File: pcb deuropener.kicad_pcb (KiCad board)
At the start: 2 copper layers, 54.6 x 86.4 mm, 34 parts, among them J1 Conn_01x02, J10 Conn_01x03, J11 Barrel_Jack_Switch, J12 Conn_01x08, J13 Conn_01x02, J14 Conn_01x02, J2 Conn_01x02, J3 Conn_01x02, J4 Conn_01x02, J5 Conn_01x02, P8 BeagleBone_Black_Header, P9 BeagleBone_Black_Header, Q1 STU60N3LH5, Q2 STU60N3LH5, U1 TSR_1-2450

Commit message: A lot of changes for rev0.02 and fix for issue #2
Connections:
- net IO-P8_13-UI_TriLED1r renamed IO-P8_13-UI_DuoLED1r
- net IO-P8_19-UI_TriLED1g renamed IO-P8_19-UI_DuoLED1g
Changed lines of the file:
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@@
   (net 25 IO-P8_18-Button2)
   (net 26 IO-P8_17-Button1)
-  (net 27 IO-P8_19-UI_TriLED1g)
-  (net 28 IO-P8_13-UI_TriLED1r)
+  (net 27 IO-P8_19-UI_DuoLED1g)
+  (net 28 IO-P8_13-UI_DuoLED1r)
   (net 29 IO-P8_09-Buzzer)
   (net 30 IO-P9_16-UILED2)
@@
     (add_net Earth)
     (add_net IO-P8_09-Buzzer)
-    (add_net IO-P8_13-UI_TriLED1r)
+    (add_net IO-P8_13-UI_DuoLED1r)
     (add_net IO-P8_17-Button1)
     (add_net IO-P8_18-Button2)
-    (add_net IO-P8_19-UI_TriLED1g)
+    (add_net IO-P8_19-UI_DuoLED1g)
     (add_net IO-P9_12-Solenoid)
     (add_net IO-P9_14-UILED1)
@@
     (pad 20 thru_hole oval (at 2.54 22.86) (size 1.7272 1.7272) (drill 1.016) (layers *.Cu *.Mask F.SilkS))
     (pad 19 thru_hole oval (at 0 22.86) (size 1.7272 1.7272) (drill 1.016) (layers *.Cu *.Mask F.SilkS)
-      (net 27 IO-P8_19-UI_TriLED1g))
+      (net 27 IO-P8_19-UI_DuoLED1g))
     (pad 18 thru_hole oval (at 2.54 20.32) (size 1.7272 1.7272) (drill 1.016) (layers *.Cu *.Mask F.SilkS)
       (net 25 IO-P8_18-Button2))
@@
     (pad 14 thru_hole oval (at 2.54 15.24) (size 1.7272 1.7272) (drill 1.016) (layers *.Cu *.Mask F.SilkS))
     (pad 13 thru_hole oval (at 0 15.24) (size 1.7272 1.7272) (drill 1.016) (layers *.Cu *.Mask F.SilkS)
-      (net 28 IO-P8_13-UI_TriLED1r))
+      (net 28 IO-P8_13-UI_DuoLED1r))
     (pad 12 thru_hole oval (at 2.54 12.7) (size 1.7272 1.7272) (drill 1.016) (layers *.Cu *.Mask F.SilkS))
     (pad 11 thru_hole oval (at 0 12.7) (size 1.7272 1.7272) (drill 1.016) (layers *.Cu *.Mask F.SilkS))
@@
     (fp_line (start 1.93 -1.25) (end 1.93 1.25) (layer F.Fab) (width 0.1))
     (pad 2 thru_hole oval (at 10.16 0 90) (size 1.6 1.6) (drill 0.8) (layers *.Cu *.Mask)
-      (net 28 IO-P8_13-UI_TriLED1r))
+      (net 28 IO-P8_13-UI_DuoLED1r))
     (pad 1 thru_hole circle (at 0 0 90) (size 1.6 1.6) (drill 0.8) (layers *.Cu *.Mask)
       (net 12 "Net-(J10-Pad1)"))
@@
     (fp_line (start 1.93 -1.25) (end 1.93 1.25) (layer F.Fab) (width 0.1))
     (pad 2 thru_hole oval (at 10.16 0 90) (size 1.6 1.6) (drill 0.8) (layers *.Cu *.Mask)
-      (net 27 IO-P8_19-UI_TriLED1g))
+      (net 27 IO-P8_19-UI_DuoLED1g))
     (pad 1 thru_hole circle (at 0 0 90) (size 1.6 1.6) (drill 0.8) (layers *.Cu *.Mask)
       (net 13 "Net-(J10-Pad3)"))

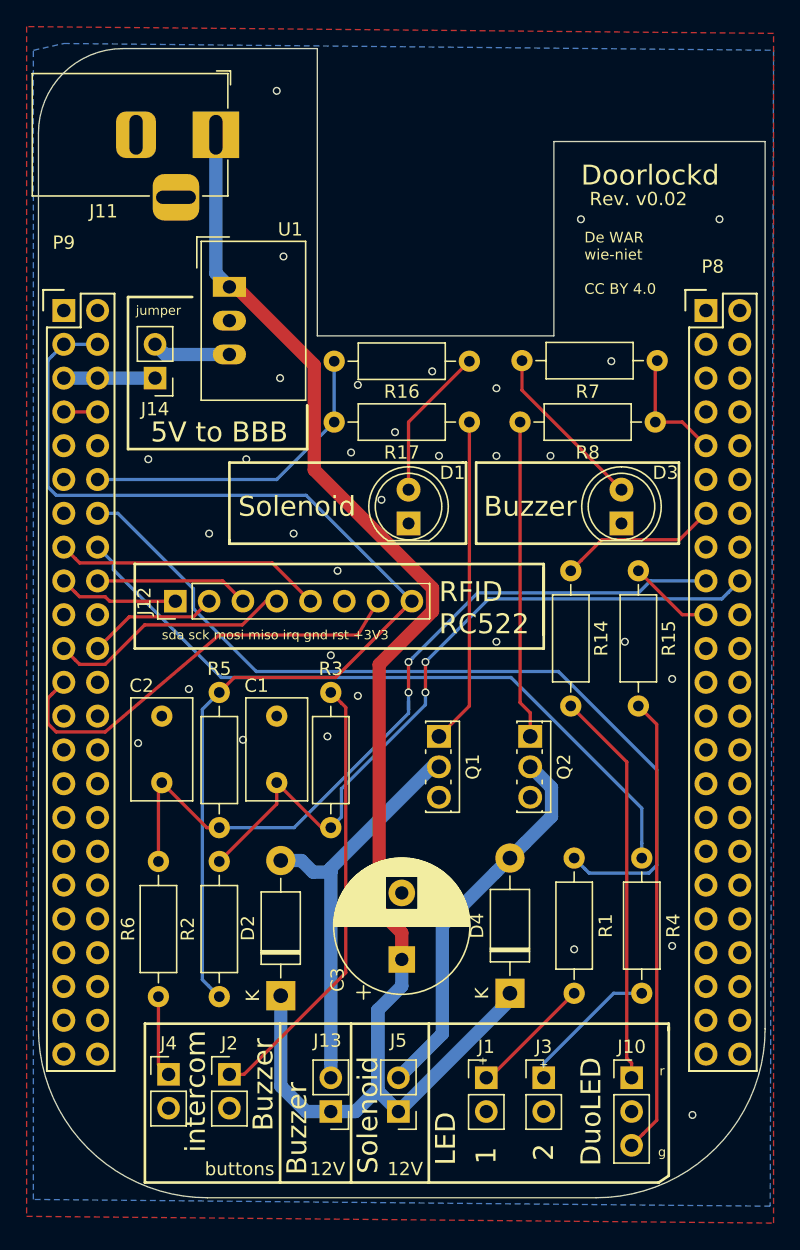
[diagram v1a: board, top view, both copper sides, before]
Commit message: Better Earth track to FETs and Capacitor
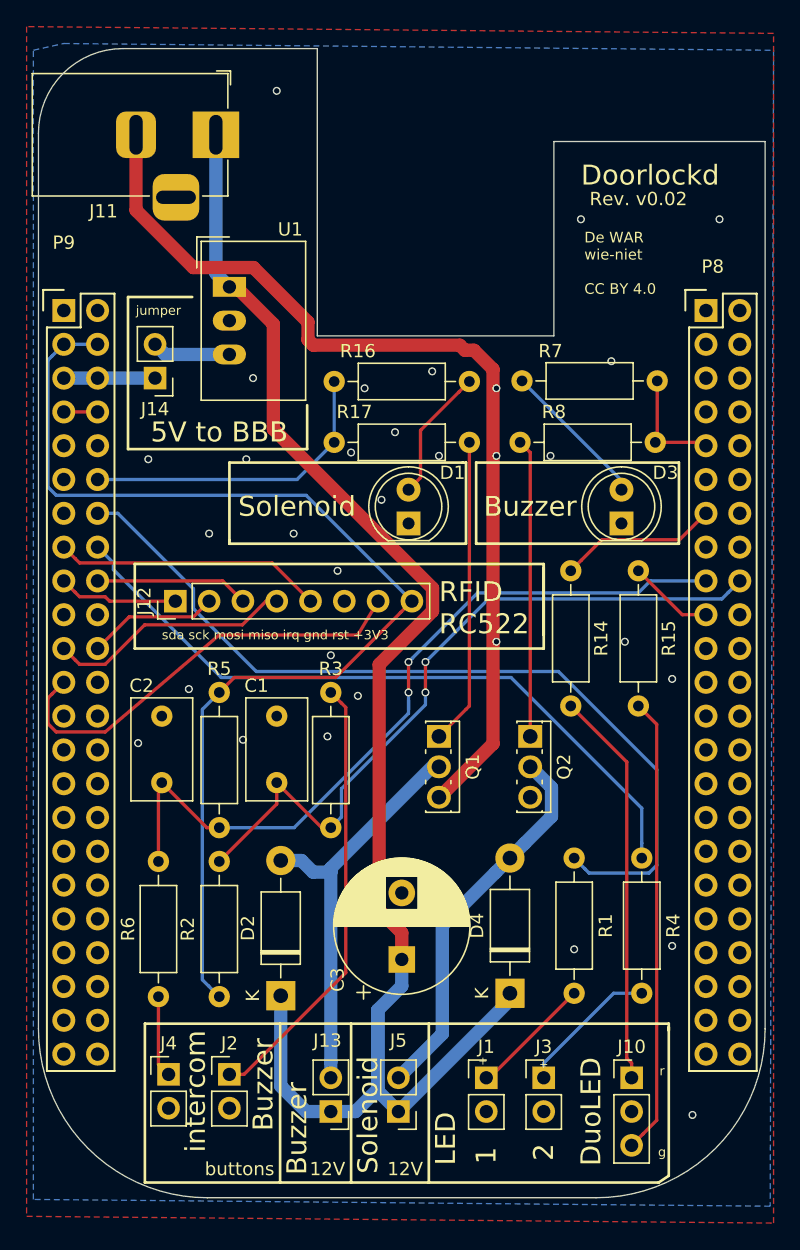
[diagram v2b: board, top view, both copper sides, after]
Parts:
- moved R17 1.52 mm to (136.7, 72.3)
- moved R7 1.52 mm to (161.0, 67.7)
- moved R8 1.52 mm to (160.8, 72.3)
- moved R16 1.52 mm to (136.7, 67.7)
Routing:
- net Earth: track 0.00 -> 72.1 mm, vias 32 -> 31
- net Net-(D3-Pad2): track 12.8 -> 11.3 mm
- net Net-(Q2-Pad1): track 23.9 -> 22.4 mm
- net Net-(Q1-Pad1): track 24.6 -> 23.0 mm
- net Net-(D1-Pad2): track 11.5 -> 10.0 mm
- net IO-P8_09-Buzzer: track 9.43 -> 8.59 mm
- net IO-P9_12-Solenoid: track 24.1 -> 23.5 mm

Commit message: improved Earth path and 12V path to the southern area of the pcb.
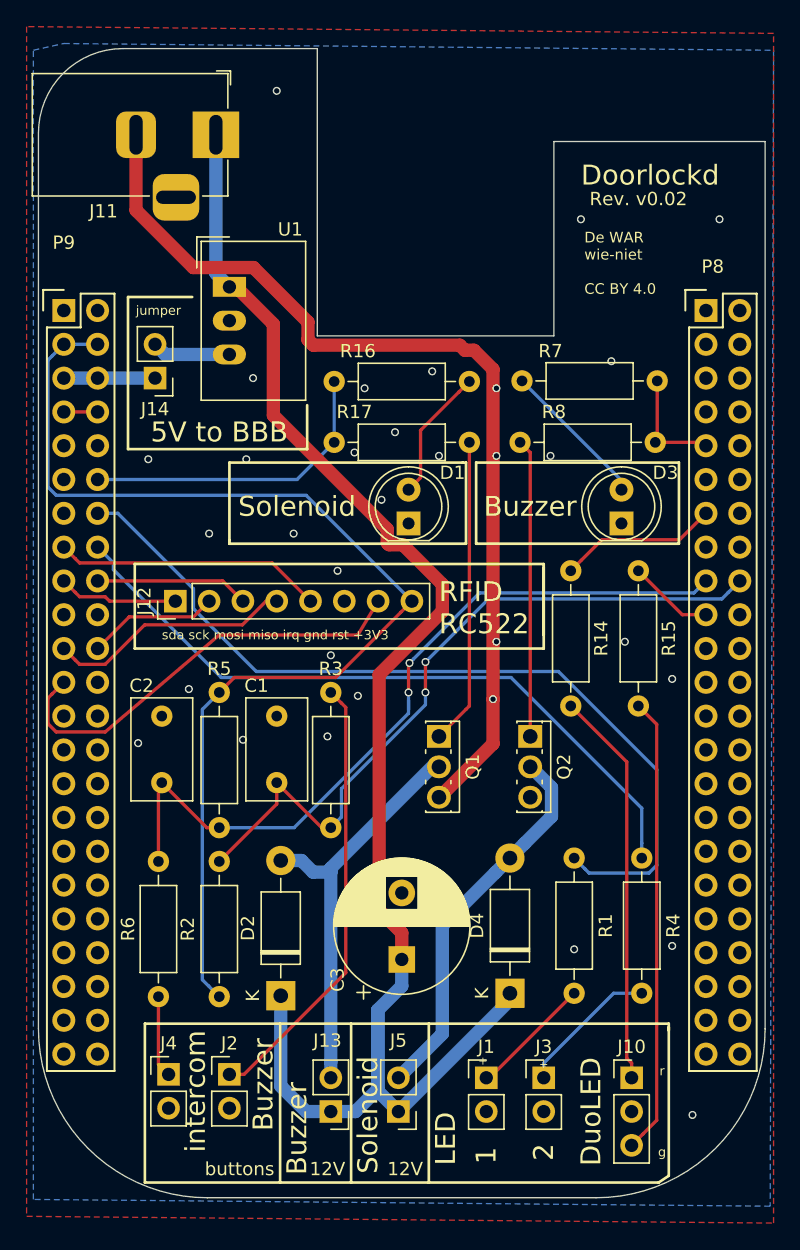
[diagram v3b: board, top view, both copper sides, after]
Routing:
- net +12V: track 118.1 -> 119.3 mm
- net Earth: vias 31 -> 32
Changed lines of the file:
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@@
     (thickness 1.6)
     (drawings 63)
-    (tracks 229)
+    (tracks 235)
     (zones 0)
     (modules 34)
@@
   )
   (setup
-    (last_trace_width 0.25)
+    (last_trace_width 1)
     (user_trace_width 1)
     (trace_clearance 0.2)
@@
   (via (at 138.9761 68.2244) (size 0.6) (drill 0.4) (layers F.Cu B.Cu) (net 4))
   (via (at 144.0561 66.9544) (size 0.6) (drill 0.4) (layers F.Cu B.Cu) (net 4))
-  (via (at 137.9601 73.0504) (size 0.6) (drill 0.4) (layers F.Cu B.Cu) (net 4))
+  (via (at 138.2141 73.0504) (size 0.6) (drill 0.4) (layers F.Cu B.Cu) (net 4))
   (via (at 140.2461 76.6064) (size 0.6) (drill 0.4) (layers F.Cu B.Cu) (net 4))
   (via (at 141.2621 71.5264) (size 0.6) (drill 0.4) (layers F.Cu B.Cu) (net 4))
   (via (at 130.5941 67.4624) (size 0.6) (drill 0.4) (layers F.Cu B.Cu) (net 4))
   (segment (start 144.60685 98.9584) (end 144.5641 98.9584) (width 1) (layer F.Cu) (net 4))
-  (segment (start 148.6281 66.80366) (end 148.6281 94.93715) (width 1) (layer F.Cu) (net 4))
+  (segment (start 148.6281 66.80366) (end 148.6281 91.5924) (width 1) (layer F.Cu) (net 4))
   (segment (start 147.191831 65.367391) (end 148.6281 66.80366) (width 1) (layer F.Cu) (net 4))
   (segment (start 130.626101 59.154399) (end 134.71882 63.247118) (width 1) (layer F.Cu) (net 4))
@@
   (segment (start 121.8001 54.8518) (end 126.102699 59.154399) (width 1) (layer F.Cu) (net 4))
   (segment (start 121.8001 49.1744) (end 121.8001 54.8518) (width 1) (layer F.Cu) (net 4))
+  (segment (start 148.6281 91.5924) (end 148.6281 94.93715) (width 1) (layer F.Cu) (net 4))
+  (via (at 148.6281 91.5924) (size 0.6) (drill 0.4) (layers F.Cu B.Cu) (net 4))
   (segment (start 146.050101 68.516399) (end 146.8501 67.7164) (width 0.25) (layer F.Cu) (net 5))
   (segment (start 143.178099 71.388401) (end 146.050101 68.516399) (width 0.25) (layer F.Cu) (net 5))
@@
   (segment (start 149.8981 113.6904) (end 149.8981 114.1984) (width 1) (layer B.Cu) (net 6))
   (segment (start 149.8981 114.1984) (end 141.5161 122.5804) (width 1) (layer B.Cu) (net 6))
-  (segment (start 140.070099 88.982403) (end 140.070099 107.450399) (width 1) (layer F.Cu) (net 6))
-  (segment (start 144.082101 84.970401) (end 140.070099 88.982403) (width 1) (layer F.Cu) (net 6))
-  (segment (start 144.082101 83.248403) (end 144.082101 84.970401) (width 1) (layer F.Cu) (net 6))
-  (segment (start 132.1181 63.4064) (end 132.1181 71.284402) (width 1) (layer F.Cu) (net 6))
   (segment (start 141.7701 109.1504) (end 141.7701 111.1504) (width 1) (layer F.Cu) (net 6))
+  (segment (start 140.818099 79.984401) (end 141.846101 79.984401) (width 1) (layer F.Cu) (net 6))
+  (segment (start 140.678099 78.816399) (end 140.678099 79.844401) (width 1) (layer F.Cu) (net 6))
+  (segment (start 132.1181 70.2564) (end 140.678099 78.816399) (width 1) (layer F.Cu) (net 6))
+  (segment (start 129.3161 60.6044) (end 132.1181 63.4064) (width 1) (layer F.Cu) (net 6))
+  (segment (start 140.678099 79.844401) (end 140.818099 79.984401) (width 1) (layer F.Cu) (net 6))
+  (segment (start 140.070099 89.736401) (end 140.070099 107.450399) (width 1) (layer F.Cu) (net 6))
+  (segment (start 132.1181 63.4064) (end 132.1181 70.2564) (width 1) (layer F.Cu) (net 6))
+  (segment (start 128.8161 60.6044) (end 129.3161 60.6044) (width 1) (layer F.Cu) (net 6))
   (segment (start 140.070099 107.450399) (end 141.7701 109.1504) (width 1) (layer F.Cu) (net 6))
-  (segment (start 132.1181 71.284402) (end 144.082101 83.248403) (width 1) (layer F.Cu) (net 6))
-  (segment (start 129.3161 60.6044) (end 132.1181 63.4064) (width 1) (layer F.Cu) (net 6))
-  (segment (start 128.8161 60.6044) (end 129.3161 60.6044) (width 1) (layer F.Cu) (net 6))
+  (segment (start 144.8181 82.9564) (end 144.8181 84.9884) (width 1) (layer F.Cu) (net 6))
+  (segment (start 144.8181 84.9884) (end 140.070099 89.736401) (width 1) (layer F.Cu) (net 6))
+  (segment (start 141.846101 79.984401) (end 144.8181 82.9564) (width 1) (layer F.Cu) (net 6))
   (segment (start 136.4361 118.838319) (end 136.4361 120.0404) (width 1) (layer B.Cu) (net 7))
   (segment (start 136.4361 104.58915) (end 136.4361 118.838319) (width 1) (layer B.Cu) (net 7))
@@
   (segment (start 143.5481 88.7984) (end 148.292701 84.053799) (width 0.25) (layer B.Cu) (net 25))
   (segment (start 143.5481 88.7984) (end 143.5481 91.0844) (width 0.25) (layer F.Cu) (net 25))
-  (via (at 142.2781 88.7984) (size 0.6) (drill 0.4) (layers F.Cu B.Cu) (net 26))
   (via (at 142.2781 91.0844) (size 0.6) (drill 0.4) (layers F.Cu B.Cu) (net 26))
   (segment (start 127.1181 101.2444) (end 128.0541 101.2444) (width 0.25) (layer F.Cu) (net 26))
@@
   (segment (start 142.2781 92.3544) (end 142.2781 91.709401) (width 0.25) (layer B.Cu) (net 26))
   (segment (start 142.2781 92.642992) (end 142.2781 92.3544) (width 0.25) (layer B.Cu) (net 26))
-  (segment (start 142.578099 88.498401) (end 142.2781 88.7984) (width 0.25) (layer B.Cu) (net 26))
-  (segment (start 147.472711 83.603789) (end 142.578099 88.498401) (width 0.25) (layer B.Cu) (net 26))
-  (segment (start 159.551713 83.603789) (end 147.472711 83.603789) (width 0.25) (layer B.Cu) (net 26))
-  (segment (start 160.453102 82.7024) (end 159.551713 83.603789) (width 0.25) (layer B.Cu) (net 26))
-  (segment (start 164.6301 82.7024) (end 160.453102 82.7024) (width 0.25) (layer B.Cu) (net 26))
-  (segment (start 142.2781 88.7984) (end 142.2781 91.0844) (width 0.25) (layer F.Cu) (net 26))
+  (segment (start 164.6301 82.7024) (end 163.728711 83.603789) (width 0.25) (layer B.Cu) (net 26))
+  (segment (start 142.2781 88.942628) (end 142.350214 88.870514) (width 0.25) (layer F.Cu) (net 26))
+  (segment (start 142.2781 91.0844) (end 142.2781 88.942628) (width 0.25) (layer F.Cu) (net 26))
+  (segment (start 163.728711 83.603789) (end 147.616939 83.603789) (width 0.25) (layer B.Cu) (net 26))
+  (via (at 142.350214 88.870514) (size 0.6) (drill 0.4) (layers F.Cu B.Cu) (net 26))
+  (segment (start 147.616939 83.603789) (end 142.650213 88.570515) (width 0.25) (layer B.Cu) (net 26))
+  (segment (start 142.650213 88.570515) (end 142.350214 88.870514) (width 0.25) (layer B.Cu) (net 26))
   (segment (start 162.8521 85.2424) (end 159.5501 81.9404) (width 0.25) (layer F.Cu) (net 27))
   (segment (start 164.6301 85.2424) (end 162.8521 85.2424) (width 0.25) (layer F.Cu) (net 27))

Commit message: Documentation file added with GPIO port information and component list with values. in info_rev0.01.txt
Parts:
- C1, C2: value C -> 1uF
- J1: value Conn_01x02 -> LED 1
- J10: value Conn_01x03 -> Duo LED
- J12: value Conn_01x08 -> RFID RC522
- J13: value Conn_01x02 -> Solenoid 12V
- J14: value Conn_01x02 -> jumper
- J2: value Conn_01x02 -> Button 2
- J3: value Conn_01x02 -> LED 2
- J4: value Conn_01x02 -> Button 1
- J5: value Conn_01x02 -> Buzzer 12V
- R1: value R -> Ω LED1
- R14, R15: value R -> Ω DuoLED
- R16, R7: value R -> 100
- R17, R8: value R -> 2k2
- R2, R5: value R -> pull_up
- R3, R6: value R -> 220
- R4: value R -> Ω LED2

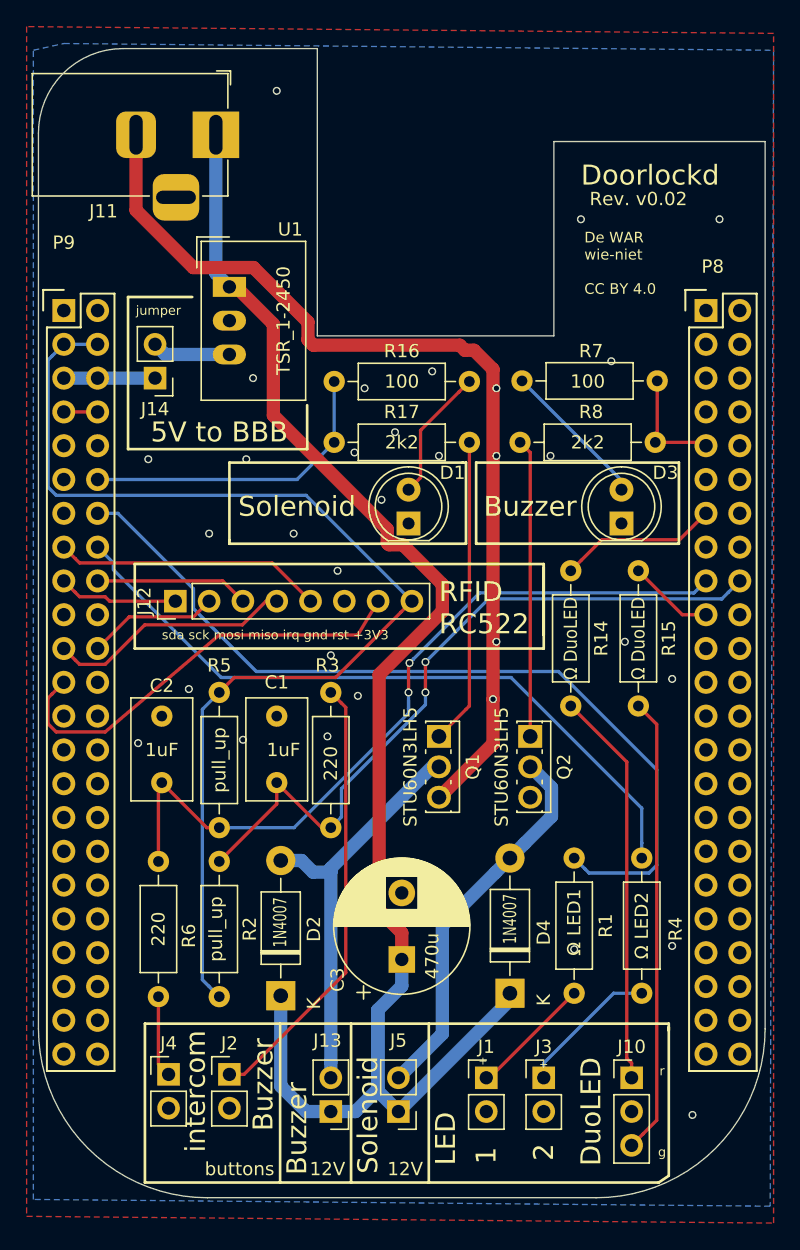
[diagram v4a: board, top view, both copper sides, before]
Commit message: fixed mix up of printed names "Solenoid" and "Buzzer". nothing changed to electronics #3
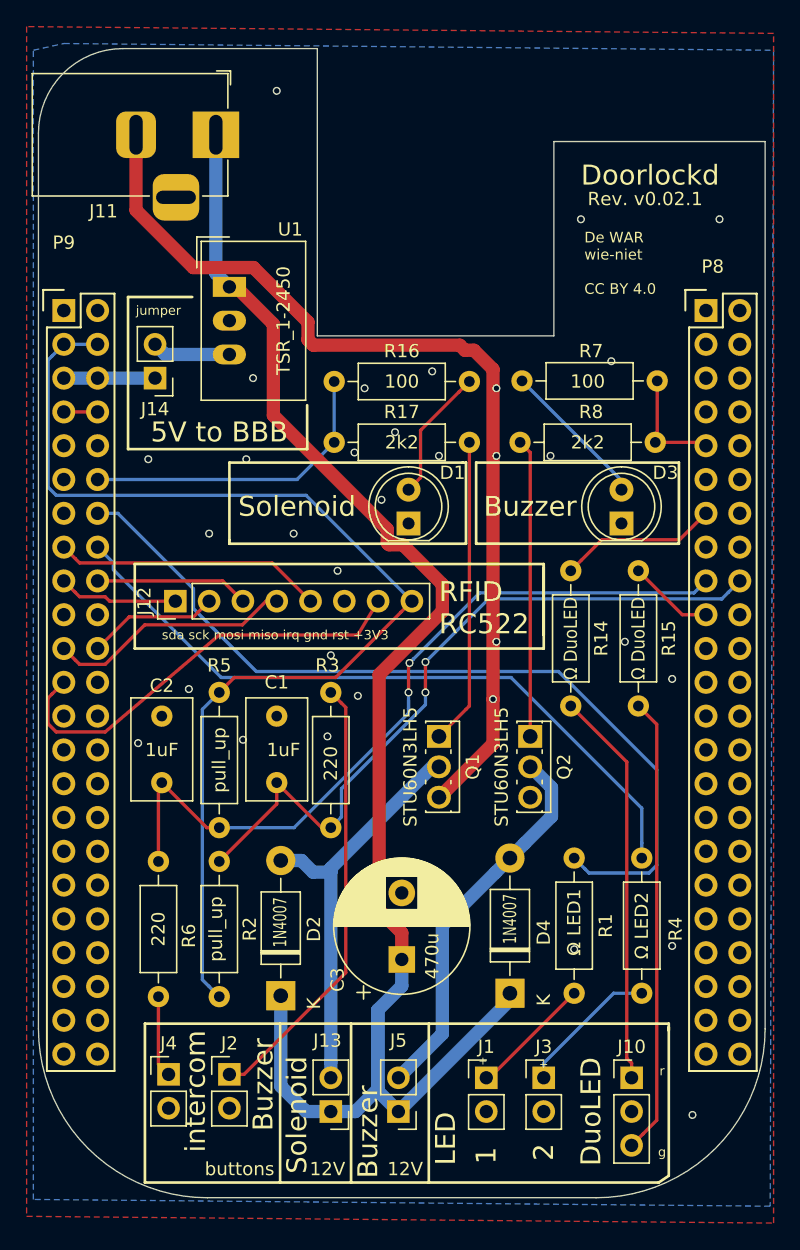
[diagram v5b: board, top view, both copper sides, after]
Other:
- board text added: "Rev. v0.02.1"
- board text removed: "Rev. v0.02"
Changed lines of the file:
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@@
     (title "Doorlockd - BBB PCB")
     (date 2019-06-11)
-    (rev v0.02)
+    (rev v0.02.1)
     (comment 1 "author: Diederik Hamelink")
     (comment 2 "CC BY 4.0")
@@
   (gr_line (start 143.8021 115.9764) (end 143.8021 127.9144) (layer F.SilkS) (width 0.2))
   (gr_line (start 137.9601 127.9144) (end 137.9601 115.9764) (layer F.SilkS) (width 0.2))
-  (gr_text "Solenoid\n" (at 139.2301 122.8344 90) (layer F.SilkS)
+  (gr_text "Solenoid\n" (at 133.8961 122.8344 90) (layer F.SilkS)
     (effects (font (size 1.5 1.5) (thickness 0.3)))
   )
-  (gr_text Buzzer (at 133.8961 123.8504 90) (layer F.SilkS)
+  (gr_text Buzzer (at 139.2301 124.1044 90) (layer F.SilkS)
     (effects (font (size 1.5 1.5) (thickness 0.3)))
   )
@@
   )
   (gr_line (start 161.0741 127.9144) (end 161.8361 127.4064) (layer F.SilkS) (width 0.2))
-  (gr_text "Rev. v0.02" (at 159.5501 54.0004) (layer F.SilkS)
+  (gr_text "Rev. v0.02.1" (at 160.0581 54.0004) (layer F.SilkS)
     (effects (font (size 1 1) (thickness 0.25)))
   )
